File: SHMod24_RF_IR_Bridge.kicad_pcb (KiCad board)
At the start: 2 copper layers, 45 x 45 mm, 4 parts, among them J1 Conn_02x14_Odd_Even

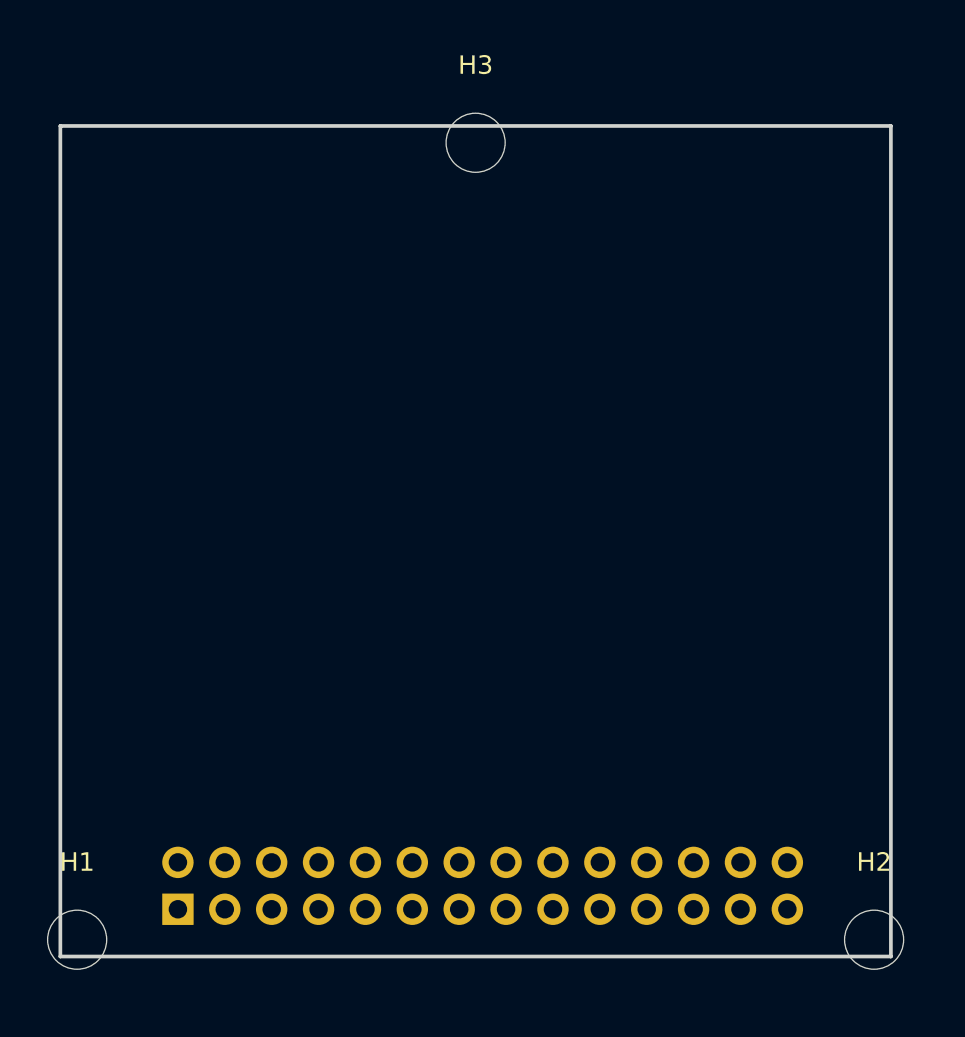
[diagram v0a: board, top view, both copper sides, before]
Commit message: add smd pin header option
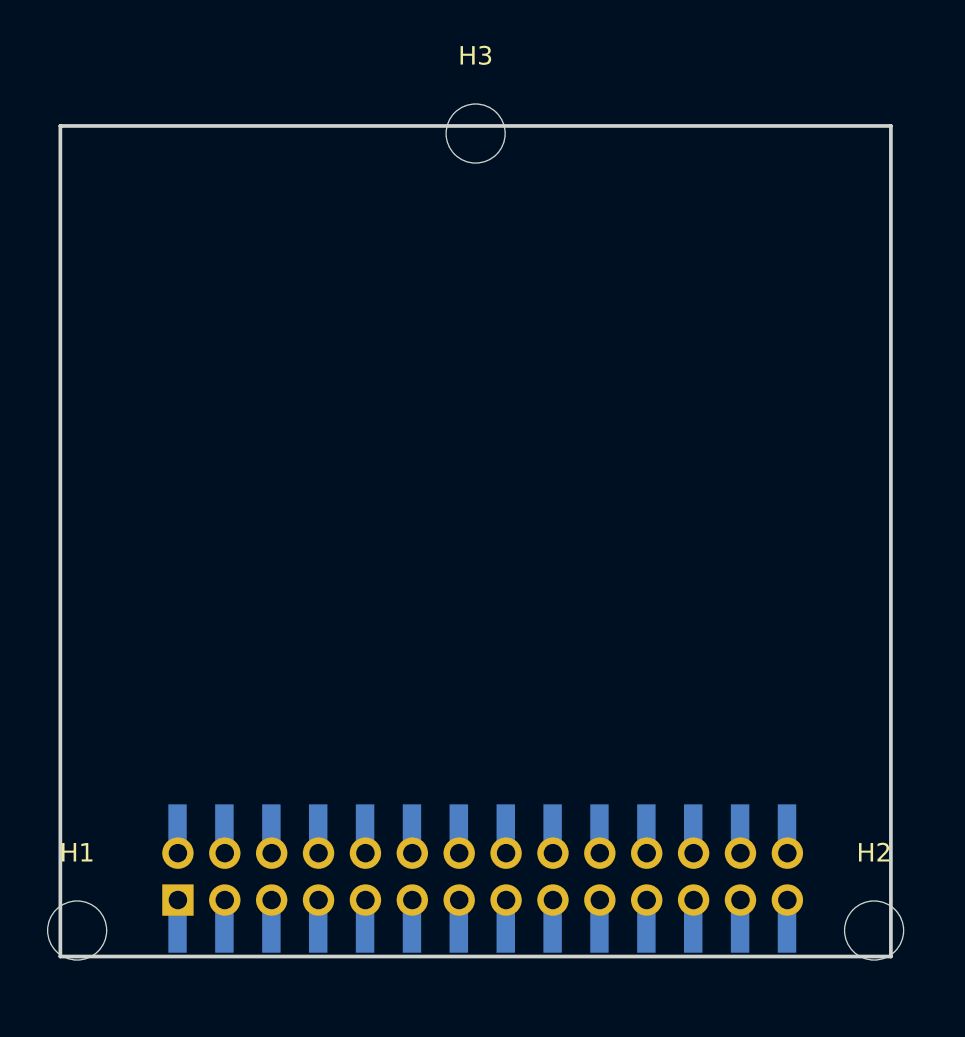
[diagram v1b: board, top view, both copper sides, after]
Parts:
- added J2: Conn_02x14_Odd_Even, Connector_PinSocket_2.54mm:PinSocket_2x14_P2.54mm_Vertical_SMD, B.Cu at (22.9, 40.8)
- J1: footprint leodj-kicad:PinSocket_2x14_P2.54mm_Vertical -> LeoDJ-kicad:PinSocket_2x14_P2.54mm_Vertical
- moved H1 0.50 mm to (0.91, 43.6)
- moved H2 0.50 mm to (44.1, 43.6)
- moved H3 0.50 mm to (22.5, 0.41)
- moved J1 0.50 mm to (22.9, 40.7)

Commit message: design IR send / receive
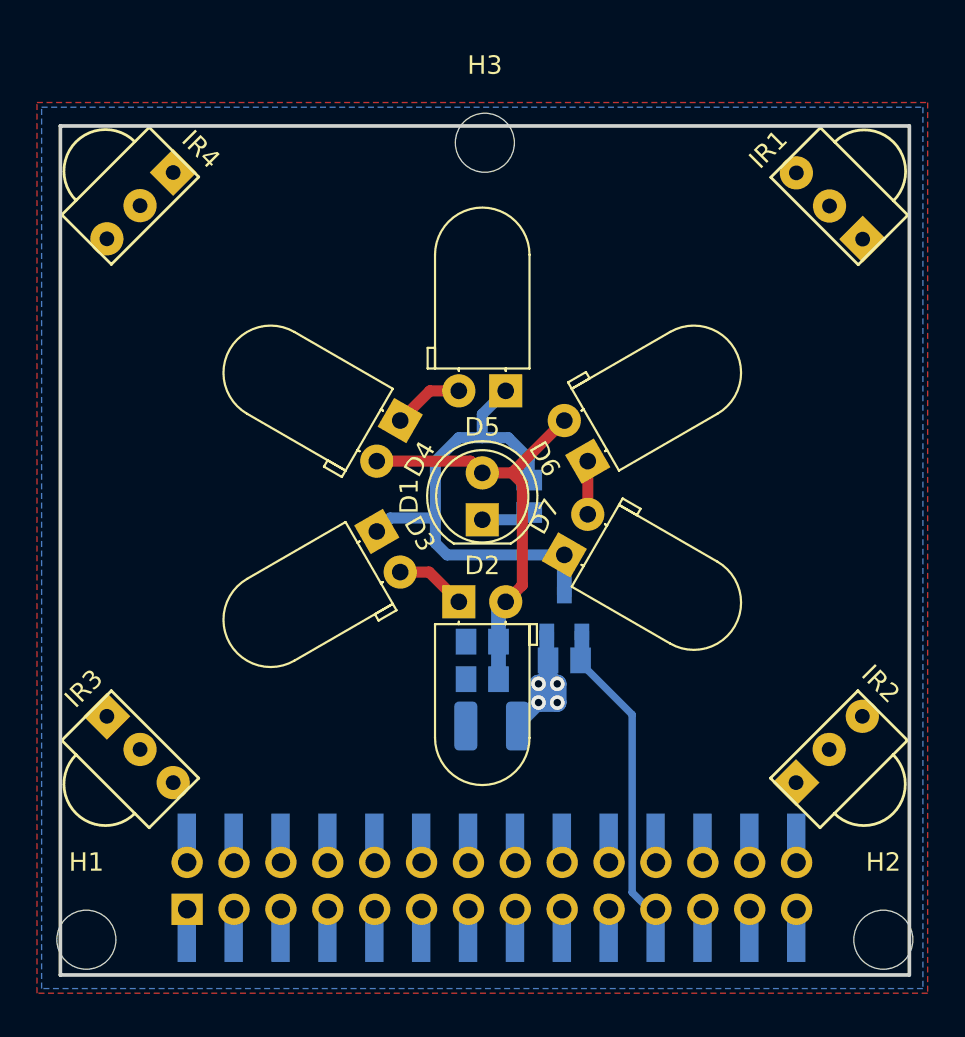
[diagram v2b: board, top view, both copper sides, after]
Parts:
- added C1: 22u, Capacitor_SMD:C_1210_3225Metric, B.Cu at (23.4, 32.5)
- added D1: LED, LED_THT:LED_D5.0mm_IRBlack, F.Cu at (22.9, 21.3)
- added D2: LED, LED_THT:LED_D5.0mm_Horizontal_O1.27mm_Z9.0mm, F.Cu at (21.6, 25.8)
- added D3: LED, LED_THT:LED_D5.0mm_Horizontal_O1.27mm_Z9.0mm, F.Cu at (17.1, 22.0)
- added D4: LED, LED_THT:LED_D5.0mm_Horizontal_O1.27mm_Z9.0mm, F.Cu at (18.4, 16.0)
- added D5: LED, LED_THT:LED_D5.0mm_Horizontal_O1.27mm_Z9.0mm, F.Cu at (24.1, 14.4)
- added D6: LED, LED_THT:LED_D5.0mm_Horizontal_O1.27mm_Z9.0mm, F.Cu at (28.6, 18.2)
- added D7: LED, LED_THT:LED_D5.0mm_Horizontal_O1.27mm_Z9.0mm, F.Cu at (27.3, 23.2)
- added IR1: VS1838b, LeoDJ-kicad:VS1838b, F.Cu at (41.7, 4.34)
- added IR2: VS1838b, LeoDJ-kicad:VS1838b, F.Cu at (41.7, 33.8)
- added IR3: VS1838b, LeoDJ-kicad:VS1838b, F.Cu at (4.32, 33.8)
- added IR4: VS1838b, LeoDJ-kicad:VS1838b, F.Cu at (4.32, 4.32)
- added Q1: AO3400A, Package_TO_SOT_SMD:SOT-23, B.Cu at (27.3, 26.4)
- added R1: R, LeoDJ-kicad:R_0805_2012Metric, B.Cu at (25.4, 20.1)
- added R2: 10k, LeoDJ-kicad:R_0805_2012Metric, B.Cu at (27.3, 29.0)
- added R3: 2, LeoDJ-kicad:R_0805_2012Metric, B.Cu at (22.9, 27.9)
- added R4: 2, LeoDJ-kicad:R_0805_2012Metric, B.Cu at (22.9, 30.0)
- moved H2 0.71 mm to (44.6, 44.1)
- moved H3 0.71 mm to (23.0, 0.91)
- moved J1 0.71 mm to (23.4, 41.2)
- moved J2 0.71 mm to (23.4, 41.3)
- moved H1 0.71 mm to (1.41, 44.1)
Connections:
- J1 pad 1: Net-(J1-Pad1) -> GND
- J1 pad 10: Net-(J1-Pad10) -> SCL
- J1 pad 11: Net-(J1-Pad11) -> MISO
- J1 pad 12: Net-(J1-Pad12) -> MOSI
- J1 pad 13: Net-(J1-Pad13) -> CS
- J1 pad 14: Net-(J1-Pad14) -> SCK
- J1 pad 15: Net-(J1-Pad15) -> A1
- J1 pad 16: Net-(J1-Pad16) -> A0
- J1 pad 17: Net-(J1-Pad17) -> A3
- J1 pad 18: Net-(J1-Pad18) -> A2
- J1 pad 19: Net-(J1-Pad19) -> GND
- J1 pad 2: Net-(J1-Pad2) -> GND
- J1 pad 20: Net-(J1-Pad20) -> GND
- J1 pad 21: Net-(J1-Pad21) -> P03
- J1 pad 22: Net-(J1-Pad22) -> P02
- J1 pad 23: Net-(J1-Pad23) -> P05
- J1 pad 24: Net-(J1-Pad24) -> P04
- J1 pad 25: Net-(J1-Pad25) -> P07
- J1 pad 26: Net-(J1-Pad26) -> P06
- J1 pad 27: Net-(J1-Pad27) -> P10
- J1 pad 28: Net-(J1-Pad28) -> P09
- J1 pad 3: Net-(J1-Pad3) -> +5V
- J1 pad 4: Net-(J1-Pad4) -> VCC
- J1 pad 5: Net-(J1-Pad5) -> +3V3
- J1 pad 6: Net-(J1-Pad6) -> +3V3
- J1 pad 7: Net-(J1-Pad7) -> RX
- J1 pad 8: Net-(J1-Pad8) -> TX
- J1 pad 9: Net-(J1-Pad9) -> SDA
- J2 pad 1: Net-(J2-Pad1) -> GND
- J2 pad 10: Net-(J2-Pad10) -> SCL
- J2 pad 11: Net-(J2-Pad11) -> MISO
- J2 pad 12: Net-(J2-Pad12) -> MOSI
- J2 pad 13: Net-(J2-Pad13) -> CS
- J2 pad 14: Net-(J2-Pad14) -> SCK
- J2 pad 15: Net-(J2-Pad15) -> A1
- J2 pad 16: Net-(J2-Pad16) -> A0
- J2 pad 17: Net-(J2-Pad17) -> A3
- J2 pad 18: Net-(J2-Pad18) -> A2
- J2 pad 19: Net-(J2-Pad19) -> GND
- J2 pad 2: Net-(J2-Pad2) -> GND
- J2 pad 20: Net-(J2-Pad20) -> GND
- J2 pad 21: Net-(J2-Pad21) -> P03
- J2 pad 22: Net-(J2-Pad22) -> P02
- J2 pad 23: Net-(J2-Pad23) -> P05
- J2 pad 24: Net-(J2-Pad24) -> P04
- J2 pad 25: Net-(J2-Pad25) -> P07
- J2 pad 26: Net-(J2-Pad26) -> P06
- J2 pad 27: Net-(J2-Pad27) -> P10
- J2 pad 28: Net-(J2-Pad28) -> P09
- J2 pad 3: Net-(J2-Pad3) -> +5V
- J2 pad 4: Net-(J2-Pad4) -> VCC
- J2 pad 5: Net-(J2-Pad5) -> +3V3
- J2 pad 6: Net-(J2-Pad6) -> +3V3
- J2 pad 7: Net-(J2-Pad7) -> RX
- J2 pad 8: Net-(J2-Pad8) -> TX
- J2 pad 9: Net-(J2-Pad9) -> SDA
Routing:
- net Net-(D3-Pad1): track 0.00 -> 27.7 mm
- net Net-(D1-Pad2): track 0.00 -> 23.5 mm
- net P03: track 0.00 -> 18.1 mm
- net GND: track 0.00 -> 8.65 mm, vias 0 -> 4
- net Net-(D4-Pad1): track 0.00 -> 3.84 mm
- net Net-(D2-Pad1): track 0.00 -> 3.84 mm
- net Net-(D6-Pad1): track 0.00 -> 2.88 mm
- net Net-(D1-Pad1): track 0.00 -> 2.70 mm
- added copper zone on B.Cu, net +3V3
- added copper zone on F.Cu, net GND
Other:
- board size 45 x 45 mm -> 46 x 46 mm
- net class 0.6 added: clearance 0.2, trace_width 0.6, via_dia 0.8, via_drill 0.4

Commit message: add boost converter, IR RX, 433MHz RX/TX and labels
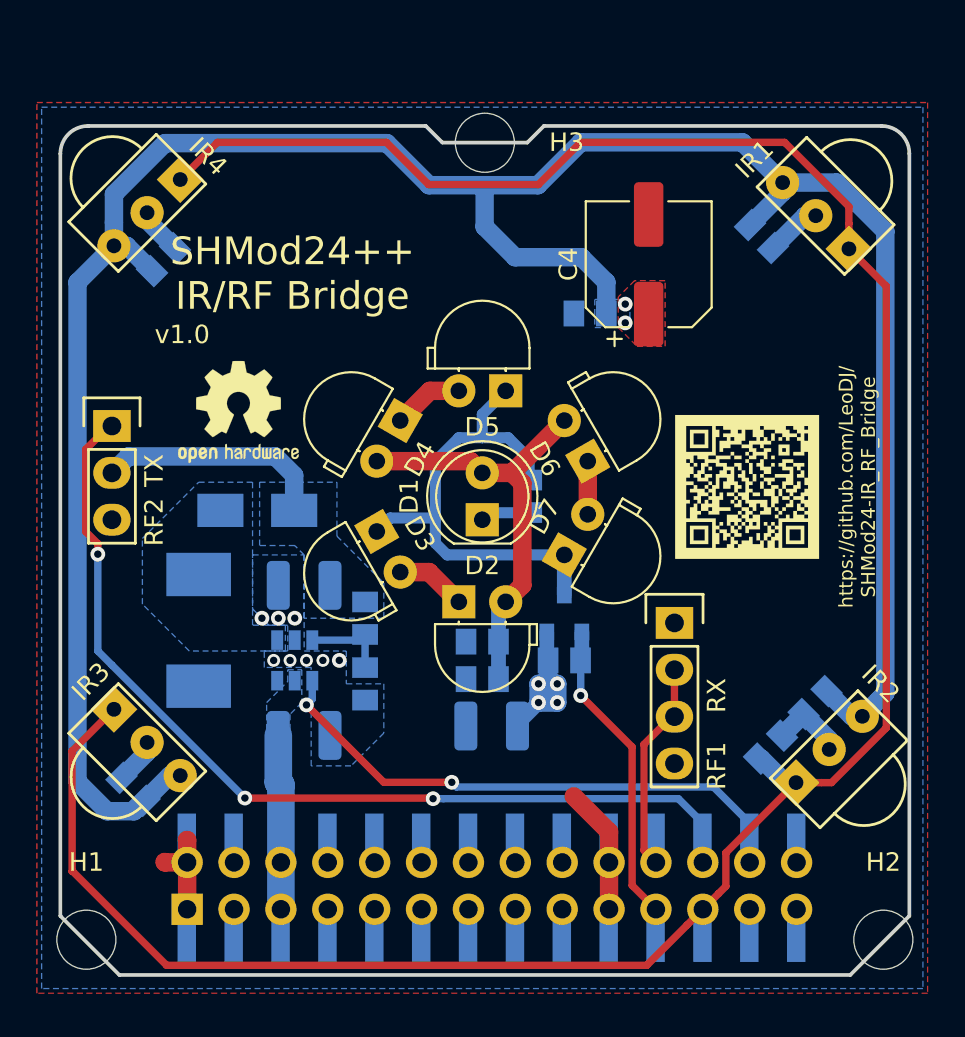
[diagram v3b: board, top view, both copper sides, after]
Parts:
- added C2: 22u, Capacitor_SMD:C_1210_3225Metric, B.Cu at (13.2, 33.0)
- added C3: 22u, Capacitor_SMD:C_1210_3225Metric, B.Cu at (13.2, 24.9)
- added C4: 100u, Capacitor_SMD:CP_Elec_6.3x5.8, F.Cu at (31.9, 7.49)
- added C6: 100n, LeoDJ-kicad:C_0805_2012Metric, B.Cu at (38.0, 5.99)
- added C7: 100n, LeoDJ-kicad:C_0805_2012Metric, B.Cu at (40.9, 31.2)
- added C8: 100n, LeoDJ-kicad:C_0805_2012Metric, B.Cu at (3.94, 35.9)
- added C9: 100n, LeoDJ-kicad:C_0805_2012Metric, B.Cu at (5.59, 7.24)
- added D8: D, Diode_SMD:D_SMA, B.Cu at (10.7, 20.8)
- added GR1: QR Code, LeoDJ-kicad:QR_Code_SHMod24-IRRF, F.Cu at (37.2, 19.6)
- added L1: 4u7, LeoDJ-kicad:L_0630, B.Cu at (7.49, 27.3)
- added LOGO1: Logo_Open_Hardware_Small, Symbol:OSHW-Logo2_7.3x6mm_SilkScreen, F.Cu at (9.65, 15.5)
- added R5: 180k, LeoDJ-kicad:R_0805_2012Metric, B.Cu at (16.5, 26.7)
- added R6: 10k, LeoDJ-kicad:R_0805_2012Metric, B.Cu at (16.5, 30.2)
- added R7: 100, LeoDJ-kicad:R_0805_2012Metric, B.Cu at (28.7, 10.2)
- added R8: 47k, LeoDJ-kicad:R_0805_2012Metric, B.Cu at (38.5, 33.7)
- added RF1: RF_Receiver_433_MHz, LeoDJ-kicad:RF_Receiver_433_MHz, F.Cu at (33.3, 32.0)
- added RF2: RF_Transmitter_433_MHz, LeoDJ-kicad:RF_Transmitter_433_MHz, F.Cu at (2.79, 18.8)
- added U1: MT3608, Package_TO_SOT_SMD:SOT-23-6, B.Cu at (12.7, 29.0)
- D2, D3, D4, D5, D6, D7: footprint LED_THT:LED_D5.0mm_Horizontal_O1.27mm_Z9.0mm -> LeoDJ-kicad:LED_D5.0mm_Horizontal_O1.27mm_Z9.0mm
- moved IR1 0.91 mm to (40.9, 4.86)
- moved IR4 0.54 mm to (4.70, 4.70)
- moved IR3 0.54 mm to (4.70, 33.4)
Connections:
- IR1 pad 1: /IR_Array/IR_rx -> P05
- IR1 pad 3: +3V3 -> +3V3-filt
- IR2 pad 1: /IR_Array/IR_rx -> P05
- IR2 pad 3: +3V3 -> +3V3-filt
- IR3 pad 1: /IR_Array/IR_rx -> P05
- IR3 pad 3: +3V3 -> +3V3-filt
- IR4 pad 1: /IR_Array/IR_rx -> P05
- IR4 pad 3: +3V3 -> +3V3-filt
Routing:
- net P05: track 0.00 -> 134.4 mm
- net +3V3-filt: track 0.00 -> 133.3 mm, vias 0 -> 2
- net P04: track 0.00 -> 50.8 mm, vias 0 -> 3
- net P06: track 0.00 -> 29.1 mm, vias 0 -> 2
- net GND: track 8.65 -> 32.8 mm, vias 4 -> 12
- net +12V: track 0.00 -> 12.7 mm
- net P02: track 0.00 -> 11.5 mm
- net +3V3: track 0.02 -> 9.50 mm
- net /Boost Converter/FB: track 0.00 -> 4.78 mm
- net P03: track 18.1 -> 16.7 mm, vias 0 -> 1
- added copper zone on B.Cu, net +12V
- added copper zone on B.Cu, net +3V3-filt
- added copper zone on F.Cu, net +3V3-filt
- added copper zone on B.Cu, net /Boost Converter/SW
- added copper zone on B.Cu, net GND
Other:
- outline, holes or cut-outs redrawn
- board text added: "RX"
- board text added: "SHMod24++ IR/RF Bridge"
- board text added: "TX"
- board text added: "https://github.com/LeoDJ/ SHMod24-IR_RF_Bridge"
- board text added: "v1.0"

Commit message: add serial comms header
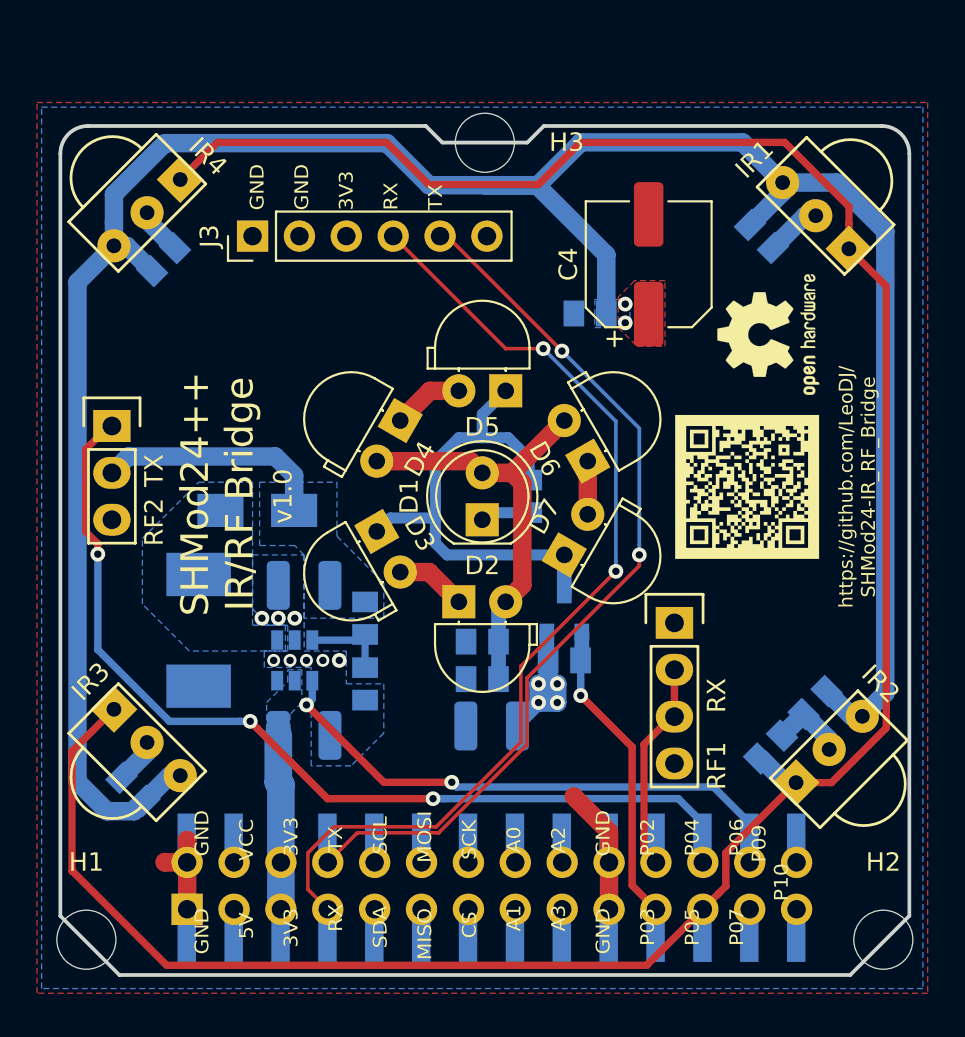
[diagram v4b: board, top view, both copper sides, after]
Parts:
- added J3: Conn_01x06, Connector_PinHeader_2.54mm:PinHeader_1x06_P2.54mm_Vertical, F.Cu at (10.4, 5.97)
- moved LOGO1 29.0 mm to (38.4, 11.3), turned to 90 degrees
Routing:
- net RX: track 0.00 -> 53.3 mm, vias 0 -> 2
- net TX: track 0.00 -> 48.2 mm, vias 0 -> 2
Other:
- net class Default: clearance 0.2 -> 0.127; trace_width 0.25 -> 0.2127
- rule trace_clearance: 0.2 -> 0.127
- rule trace_min: 0.2 -> 0.127
- rule via_min_size: 0.4 -> 0.6
- board text added: "GND GND 3V3 RX TX"
- board text added: "GND GND 5V VCC 3V3 3V3 RX TX SDA SCL MISO MOSI CS SCK A1 A0 A3 A2 GND GND P03 P02 P05 P04 P07 P06 P09 P10"

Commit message: final touches
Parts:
- added GR2: NightFury, LeoDJ-kicad:NightFury_Roll_8.0x6.1, F.Cu at (38.4, 28.6)
- moved LOGO1 0.25 mm to (38.6, 11.3)
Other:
- outline, holes or cut-outs redrawn
- board text added: "GND GND 5V VCC 3V3 3V3 RX TX SDA SCL MISO MOSI CS SCK A1 A0 A3 A2 GND GND P03 P02 P05 P04 P07 P06 ,P09 P10"
- board text removed: "GND GND 5V VCC 3V3 3V3 RX TX SDA SCL MISO MOSI CS SCK A1 A0 A3 A2 GND GND P03 P02 P05 P04 P07 P06 P09 P10"
